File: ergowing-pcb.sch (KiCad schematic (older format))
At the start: 16 parts, among them J1 USB_mini_micro_B, SW1 SW_PUSH, U1 ATMEGA32U4, X1 XTAL_GND

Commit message: Cols wired to MC
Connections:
- net row1: now also U1.10 (PB2/MOSI); no longer U1.11 (PB3/MISO)
- net row2: now also U1.9 (PB1/SCK); no longer U1.10 (PB2/MOSI)
- net row3: now also U1.8 (PB0/SS); no longer U1.9 (PB1/SCK)
- net row4: no longer U1.8 (PB0/SS)
- new net row0: U1.11 (PB3/MISO)
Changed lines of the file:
@@
 col0
 Text GLabel 2450 3650 0    60   Input ~ 0
+row0
+Text GLabel 2450 3550 0    60   Input ~ 0
 row1
-Text GLabel 2450 3550 0    60   Input ~ 0
+Text GLabel 2450 3450 0    60   Input ~ 0
 row2
-Text GLabel 2450 3450 0    60   Input ~ 0
+Text GLabel 2450 3350 0    60   Input ~ 0
 row3
-Text GLabel 2450 3350 0    60   Input ~ 0
-row4
 Text GLabel 2450 2650 0    60   Input ~ 0
 col4

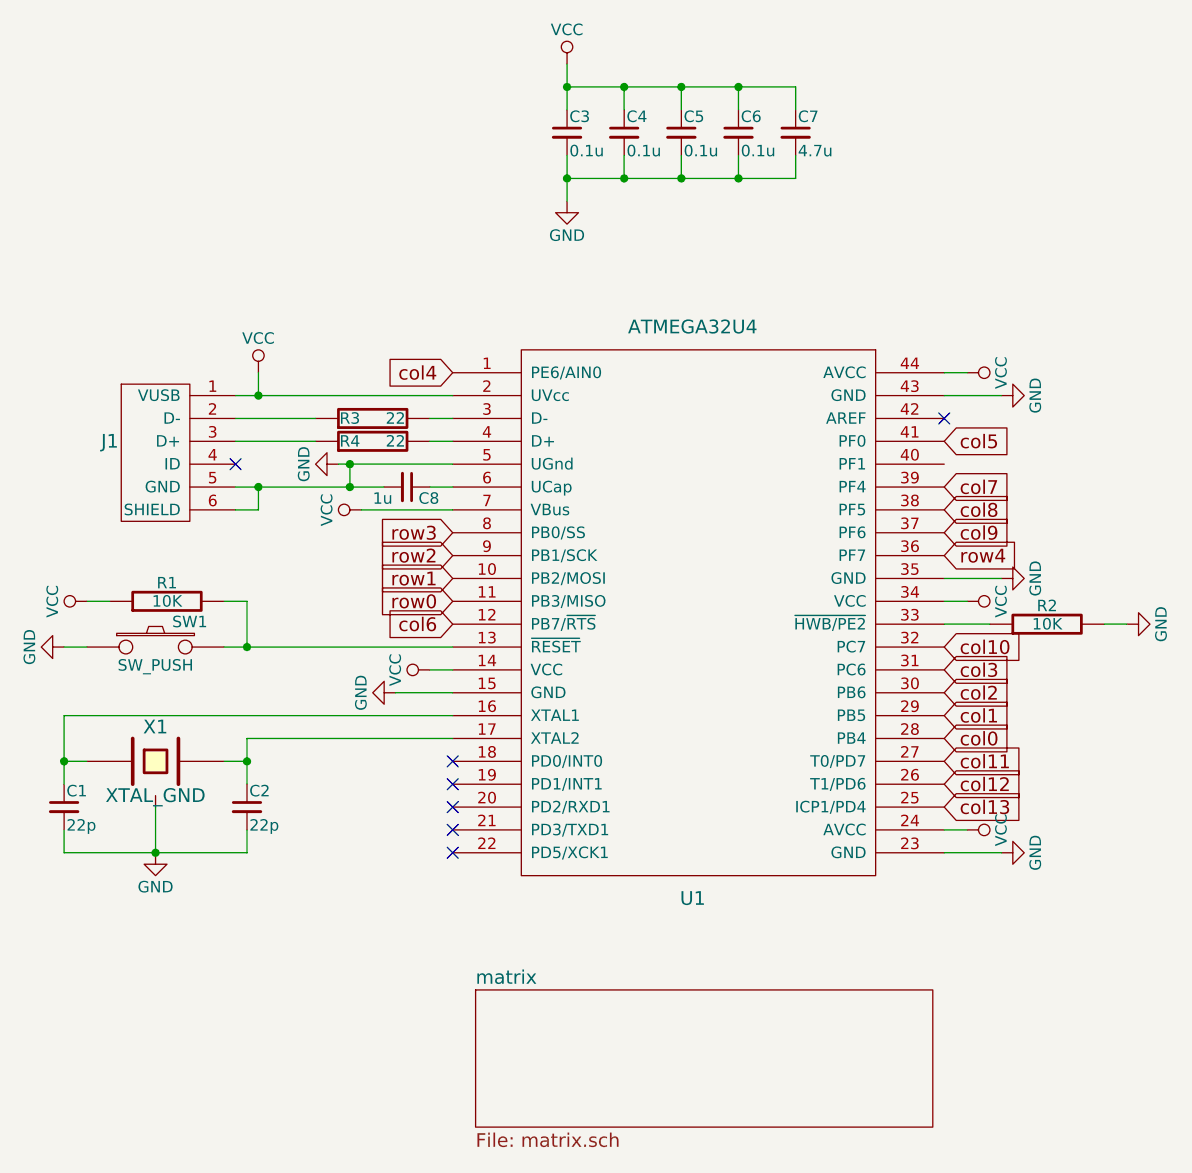
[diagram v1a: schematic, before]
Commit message: More cols wired
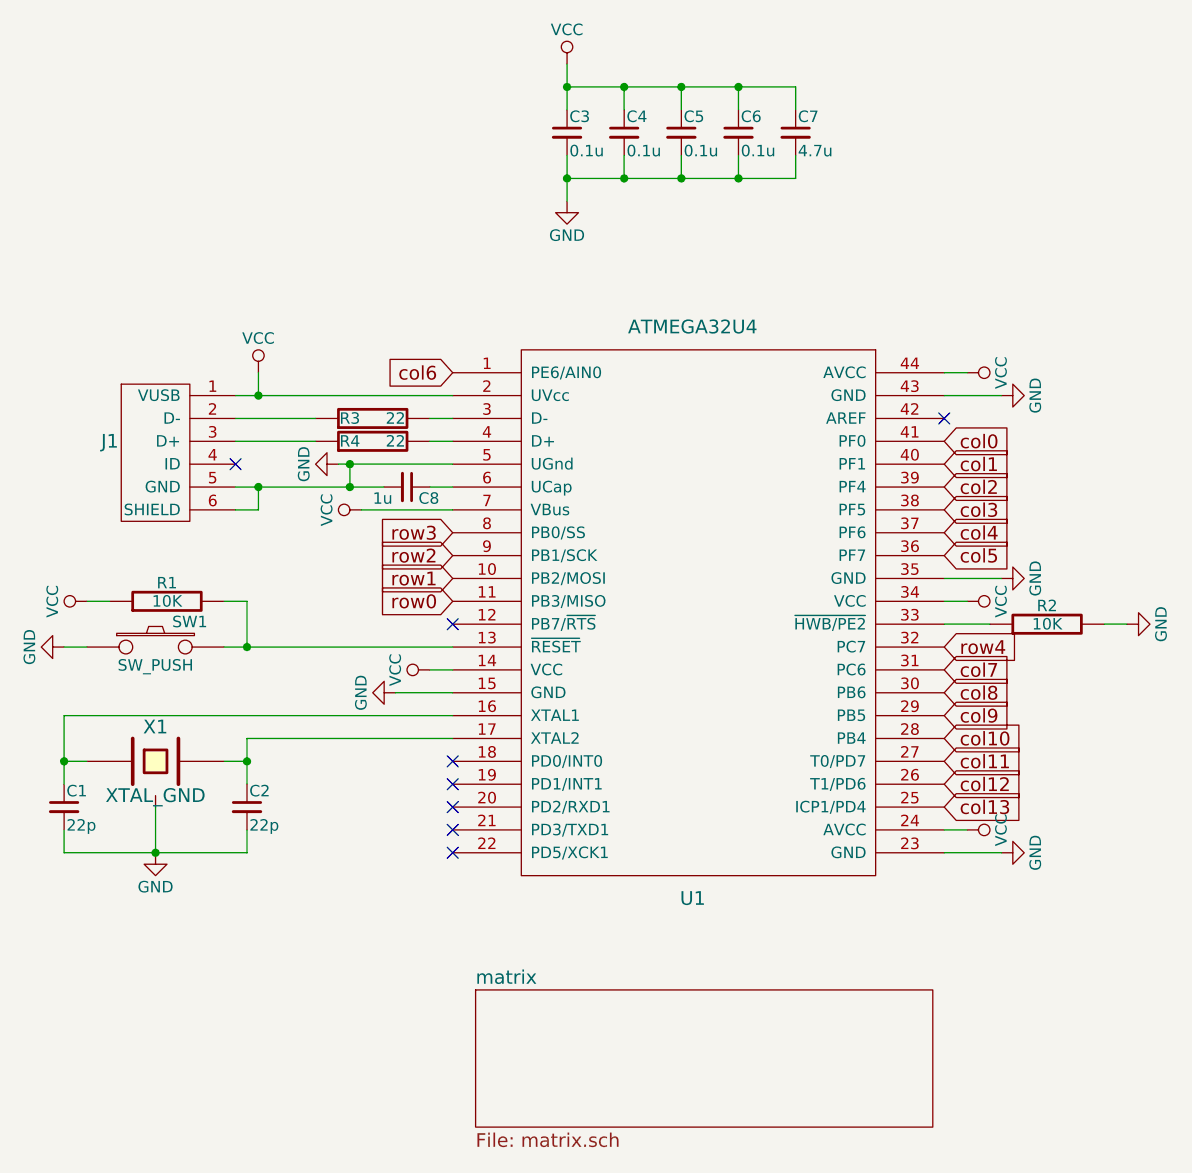
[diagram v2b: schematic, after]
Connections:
- net col0: now also U1.41 (PF0); no longer U1.28 (PB4)
- net col1: now also U1.40 (PF1); no longer U1.29 (PB5)
- net col10: now also U1.28 (PB4); no longer U1.32 (PC7)
- net col2: now also U1.39 (PF4); no longer U1.30 (PB6)
- net col3: now also U1.38 (PF5); no longer U1.31 (PC6)
- net col4: now also U1.37 (PF6); no longer U1.1 (PE6/AIN0)
- net col5: now also U1.36 (PF7); no longer U1.41 (PF0)
- net col6: now also U1.1 (PE6/AIN0); no longer U1.12 (PB7/~RTS)
- net col7: now also U1.31 (PC6); no longer U1.39 (PF4)
- net col8: now also U1.30 (PB6); no longer U1.38 (PF5)
- net col9: now also U1.29 (PB5); no longer U1.37 (PF6)
- net row4: now also U1.32 (PC7); no longer U1.36 (PF7)
- no-connect marks 7 -> 8
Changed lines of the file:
@@
 	4600 4750 4850 4750
 Text GLabel 4600 3850 2    60   Input ~ 0
-col10
+row4
 Text GLabel 4600 3950 2    60   Input ~ 0
-col3
+col7
 Text GLabel 4600 4050 2    60   Input ~ 0
-col2
-Text GLabel 4600 4150 2    60   Input ~ 0
+col8
+Text GLabel 4600 3050 2    60   Input ~ 0
 col1
 Text GLabel 4600 4250 2    60   Input ~ 0
-col0
+col10
 Text GLabel 2450 3650 0    60   Input ~ 0
 row0
@@
 row3
 Text GLabel 2450 2650 0    60   Input ~ 0
+col6
+Text GLabel 4600 2950 2    60   Input ~ 0
+col0
+Text GLabel 4600 3150 2    60   Input ~ 0
+col2
+Text GLabel 4600 3250 2    60   Input ~ 0
+col3
+Text GLabel 4600 3350 2    60   Input ~ 0
 col4
-Text GLabel 4600 2950 2    60   Input ~ 0
+Text GLabel 4600 3450 2    60   Input ~ 0
 col5
-Text GLabel 2450 3750 0    60   Input ~ 0
-col6
-Text GLabel 4600 3150 2    60   Input ~ 0
-col7
-Text GLabel 4600 3250 2    60   Input ~ 0
-col8
-Text GLabel 4600 3350 2    60   Input ~ 0
-col9
-Text GLabel 4600 3450 2    60   Input ~ 0
-row4
 Text GLabel 4600 4350 2    60   Input ~ 0
 col11
@@
 NoConn ~ 2450 4750
 NoConn ~ 4600 2850
+Text GLabel 4600 4150 2    60   Input ~ 0
+col9
+NoConn ~ 2450 3750
 $EndSCHEMATC
